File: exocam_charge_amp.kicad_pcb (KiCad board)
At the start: 2 copper layers, 20.3 x 19 mm, 13 parts, among them J1 dupont2x1, J2 dupont2x1, U1 TLV2771CDBVT

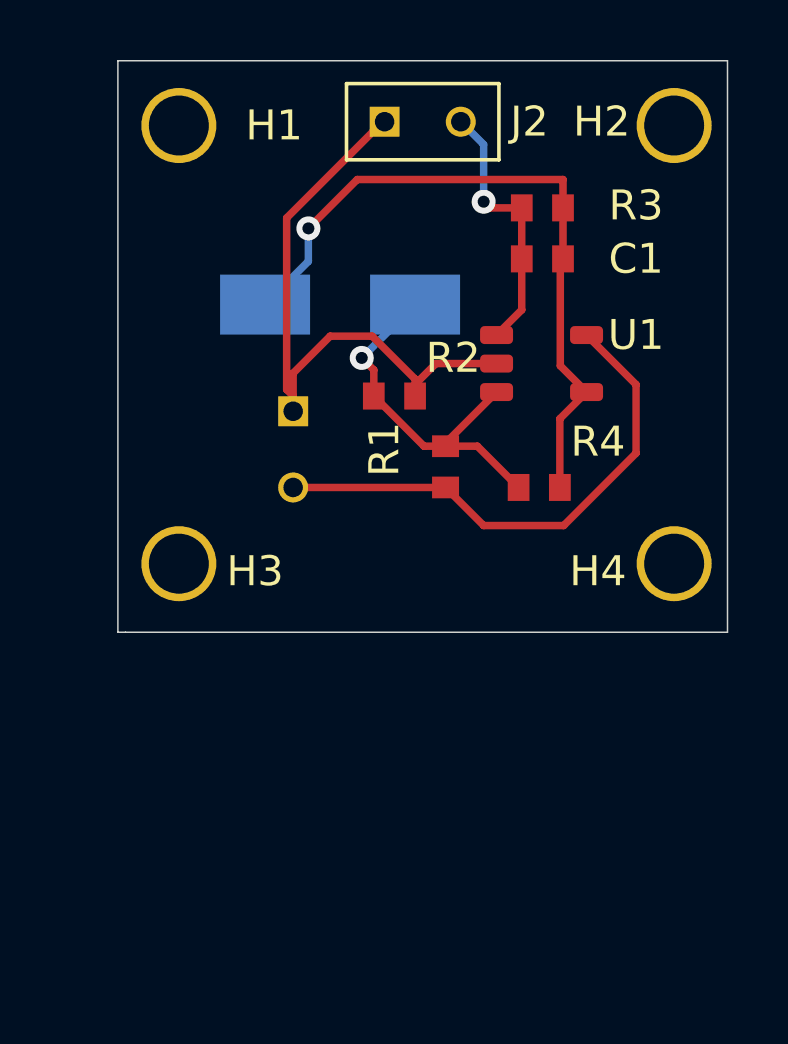
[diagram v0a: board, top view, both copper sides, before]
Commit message: updated pcb to be the new hole pattern on the shoulder side
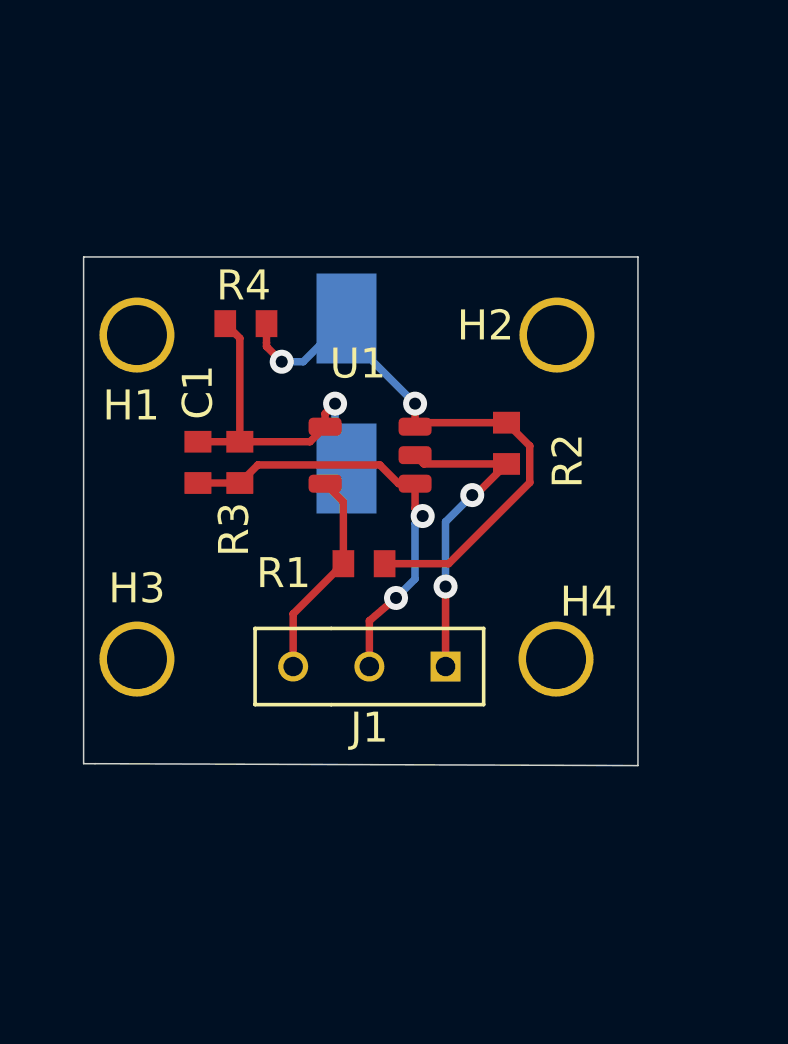
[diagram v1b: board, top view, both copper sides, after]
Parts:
- removed J2: dupont2x1, exocam_charge_amp:dupont2x1
- J1: value dupont2x1 -> dupont3x1; footprint exocam_charge_amp:dupont2x1 -> exocam_charge_amp:dupont3x1; moved to F.Cu
- moved U1 11.3 mm to (61.2, 65.9), turned to 180 degrees
- moved R4 11.0 mm to (56.3, 60.6), turned to 180 degrees
- moved J1 9.91 mm to (61.0, 72.0), turned to 180 degrees
- moved C1 9.65 mm to (57.8, 63.2), turned to 270 degrees
- moved R3 9.54 mm to (59.2, 63.2), turned to 270 degrees
- moved H2 8.00 mm to (68.5, 54.6)
- moved R2 7.38 mm to (68.1, 62.6), turned to 270 degrees
- moved H1 7.12 mm to (54.5, 54.6)
- moved H4 5.06 mm to (68.5, 65.4)
- moved H3 3.47 mm to (54.5, 65.4)
- moved BZ1 2.74 mm to (62.7, 60.3), turned to 90 degrees
- moved R1 1.33 mm to (61.4, 63.5), turned to 0 degrees
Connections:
- J1 pad 2: +5V -> Net-(C1-Pad2)
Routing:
- net Net-(BZ1-Pad1): track 23.3 -> 11.8 mm
- net +5V: track 17.6 -> 7.04 mm
- net GND: track 21.0 -> 10.8 mm, vias 0 -> 2
- net Net-(BZ1-Pad2): track 12.5 -> 20.2 mm, vias 1 -> 2
- net Net-(C1-Pad2): track 8.93 -> 14.9 mm, vias 1 -> 2
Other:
- board size 20.3 x 19 mm -> 18.5 x 17 mm

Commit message: modify board to be the two way amplification stage for higher range of outputs
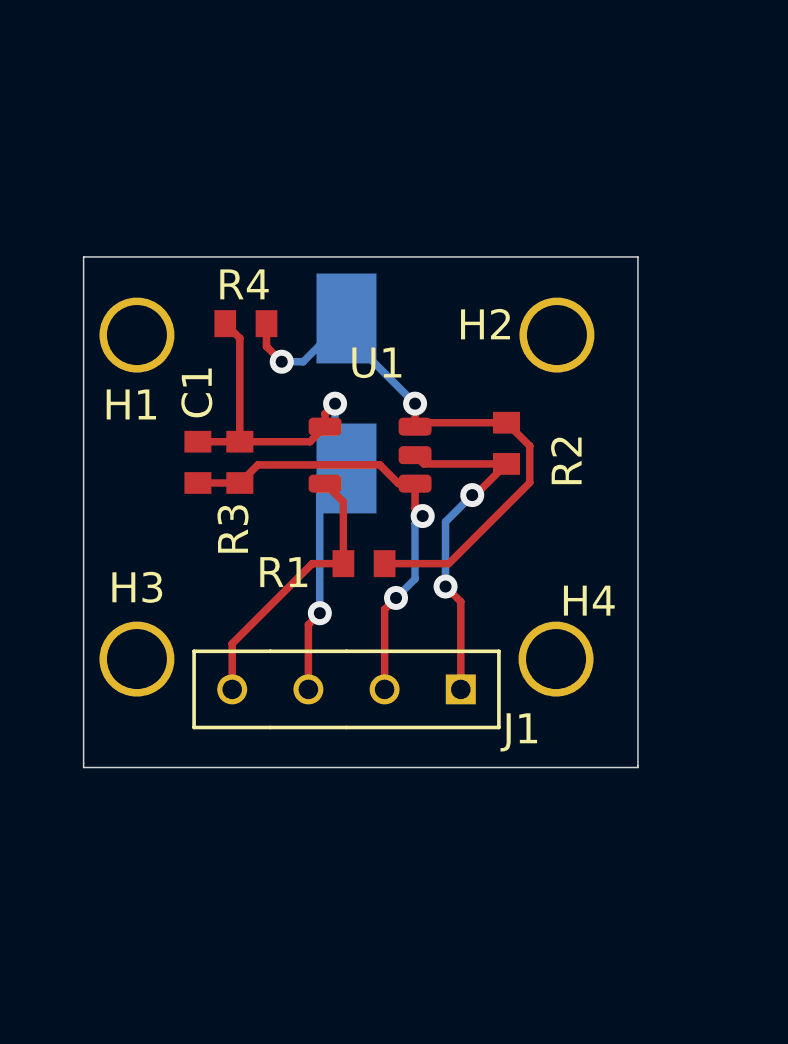
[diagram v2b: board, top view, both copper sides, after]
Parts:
- J1: value dupont3x1 -> dupont4x1; footprint exocam_charge_amp:dupont3x1 -> exocam_charge_amp:dupont4x1
- moved J1 0.92 mm to (61.5, 72.8)
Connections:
- net Net-(C1-Pad2) renamed /Amplified
- BZ1 pad 1: Net-(BZ1-Pad1) -> /UnAmplified
- C1 pad 1: Net-(BZ1-Pad1) -> /UnAmplified
- J1 pad 3: +5V -> /UnAmplified
- R3 pad 1: Net-(BZ1-Pad1) -> /UnAmplified
- R4 pad 2: Net-(BZ1-Pad1) -> /UnAmplified
- U1 pad 4: Net-(BZ1-Pad1) -> /UnAmplified
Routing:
- net /UnAmplified: track 0.00 -> 19.7 mm, vias 0 -> 2
- net Net-(BZ1-Pad1): track 11.8 -> 0.00 mm, vias 1 -> 0
- net +5V: track 7.04 -> 9.25 mm
- net GND: track 10.8 -> 11.8 mm
- net /Amplified: track 14.9 -> 15.4 mm
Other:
- outline, holes or cut-outs redrawn

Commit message: updated so that vertical distance is correct for the holes
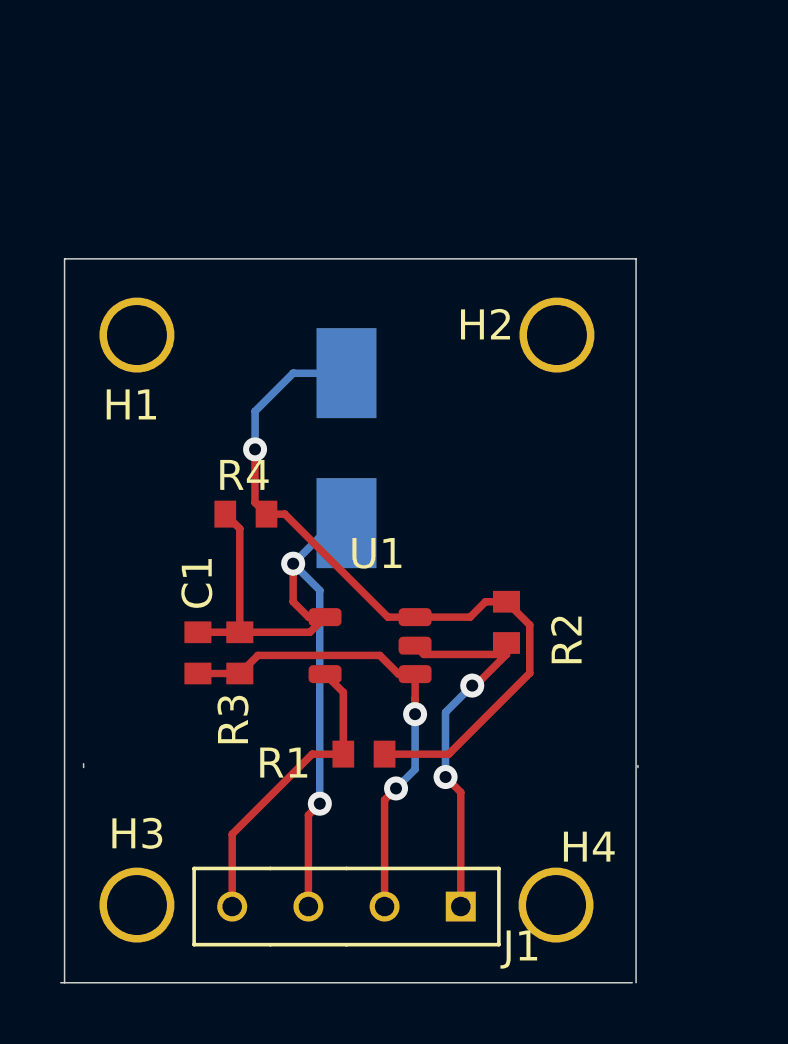
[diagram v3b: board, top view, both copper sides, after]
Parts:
- moved H3 8.20 mm to (54.5, 73.6)
- moved H4 8.20 mm to (68.5, 73.6)
- moved J1 7.24 mm to (61.5, 80.0)
- moved U1 6.35 mm to (61.2, 72.3)
- moved C1 6.35 mm to (57.8, 69.6)
- moved R3 6.35 mm to (59.2, 69.6)
- moved R4 6.35 mm to (56.3, 66.9)
- moved R1 6.35 mm to (61.4, 69.8)
- moved R2 5.97 mm to (68.1, 68.6)
- moved BZ1 1.82 mm to (62.7, 62.1)
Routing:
- net Net-(BZ1-Pad2): track 20.2 -> 26.1 mm, vias 2 -> 1
- net /UnAmplified: track 19.7 -> 25.4 mm
- net GND: track 11.8 -> 12.7 mm
- net +5V: track 9.25 -> 10.1 mm
- net /Amplified: track 15.4 -> 16.0 mm
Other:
- board size 18.5 x 17 mm -> 19.2 x 24.1 mm

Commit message: shoulder silkscreen updated
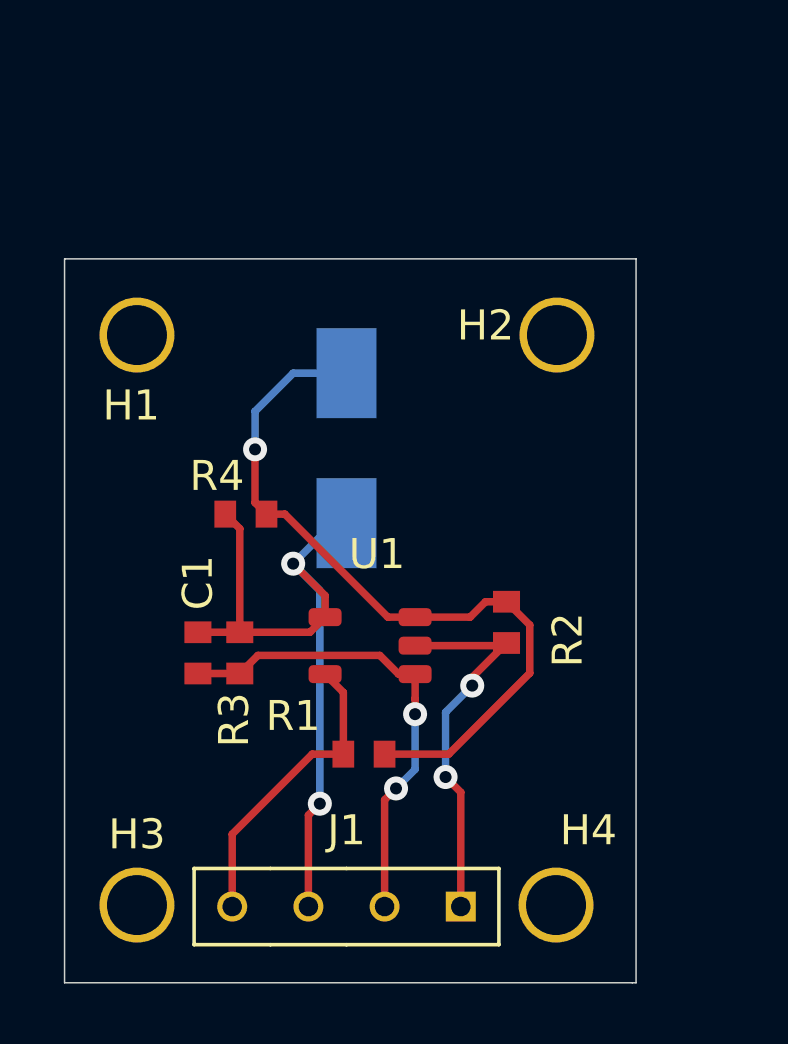
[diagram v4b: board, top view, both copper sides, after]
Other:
- board size 19.2 x 24.1 mm -> 19 x 24.1 mm
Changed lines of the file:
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@@
   (general
     (thickness 1.6)
-    (drawings 6)
+    (drawings 5)
     (tracks 69)
     (zones 0)
@@
   (module exocam_charge_amp:dupont4x1 (layer F.Cu)
     (at 61.468 80.01 180)
-    (fp_text reference J1 (at -4.572 1.2065) (layer F.SilkS)
+    (fp_text reference J1 (at 1.27 5.08) (layer F.SilkS)
       (effects (font (size 1 1) (thickness 0.15)))
     )
@@
   (module exocam_charge_amp:0603_R (layer F.Cu)
     (at 56.261 66.929 180)
-    (fp_text reference R4 (at -0.508 3.81) (layer F.SilkS)
+    (fp_text reference R4 (at 0.381 3.81) (layer F.SilkS)
       (effects (font (size 1 1) (thickness 0.15)))
     )
@@
   (module exocam_charge_amp:0603_R (layer F.Cu)
     (at 61.363 69.85)
-    (fp_text reference R1 (at -3.2605 2.8575) (layer F.SilkS)
+    (fp_text reference R1 (at -2.943 1.27) (layer F.SilkS)
       (effects (font (size 1 1) (thickness 0.15)))
     )
@@
   (module exocam_charge_amp:mount_hole_2.5mm (layer F.Cu)
     (at 68.453 73.61)
-    (fp_text reference H4 (at -0.1905 1.9) (layer F.SilkS)
+    (fp_text reference H4 (at -0.1905 1.32) (layer F.SilkS)
       (effects (font (size 1 1) (thickness 0.15)))
     )
@@
   (module exocam_charge_amp:piezo_buzzer (layer B.Cu)
     (at 62.738 62.15 90)
-    (fp_text reference BZ1 (at 2.286 0.254 90) (layer B.SilkS)
+    (fp_text reference BZ1 (at -0.08 -0.508 90) (layer B.SilkS)
       (effects (font (size 1 1) (thickness 0.15)) (justify mirror))
     )
@@
       (net 4 /UnAmplified))
   )
+  (gr_line (start 50.8 80.01) (end 69.723 80.01) (layer Edge.Cuts) (width 0.05))
+  (gr_line (start 69.723 80.01) (end 69.85 80.01) (layer Edge.Cuts) (width 0.05))
   (gr_line (start 50.8 80.01) (end 50.8 55.88) (layer Edge.Cuts) (width 0.05))
-  (gr_line (start 69.723 80.01) (end 50.673 80.01) (layer Edge.Cuts) (width 0.05))
   (gr_line (start 69.85 55.88) (end 69.85 80.01) (layer Edge.Cuts) (width 0.05))
   (gr_line (start 50.8 55.88) (end 69.85 55.88) (layer Edge.Cuts) (width 0.05))
-  (gr_line (start 69.9135 72.8345) (end 69.9135 72.771) (layer Edge.Cuts) (width 0.05))
-  (gr_line (start 51.435 72.7075) (end 51.435 72.8345) (layer Edge.Cuts) (width 0.05))
   (segment (start 62.616 67.691) (end 62.484 67.823) (width 0.25) (layer F.Cu) (net 1))
   (segment (start 64.319 67.823) (end 62.484 67.823) (width 0.25) (layer F.Cu) (net 1))
@@
   (segment (start 56.388 75.057) (end 59.055 72.39) (width 0.25) (layer F.Cu) (net 2))
   (segment (start 56.388 75.057) (end 56.388 77.47) (width 0.25) (layer F.Cu) (net 2))
-  (segment (start 62.777 69.066) (end 62.484 68.773) (width 0.25) (layer F.Cu) (net 3))
-  (segment (start 65.532 69.066) (end 62.777 69.066) (width 0.25) (layer F.Cu) (net 3))
   (segment (start 63.5 73.152) (end 63.5 73.152) (width 0.25) (layer F.Cu) (net 3))
   (via (at 63.5 73.152) (size 0.8) (drill 0.4) (layers F.Cu B.Cu) (net 3))
@@
   (segment (start 64.389 70.104) (end 64.389 70.104) (width 0.25) (layer B.Cu) (net 3))
   (via (at 64.389 70.104) (size 0.8) (drill 0.4) (layers F.Cu B.Cu) (net 3))
-  (segment (start 64.494 70.104) (end 65.532 69.066) (width 0.25) (layer F.Cu) (net 3))
   (segment (start 64.389 70.104) (end 64.494 70.104) (width 0.25) (layer F.Cu) (net 3))
   (segment (start 64.008 73.66) (end 63.5 73.152) (width 0.25) (layer F.Cu) (net 3))
   (segment (start 64.008 73.66) (end 64.008 77.47) (width 0.25) (layer F.Cu) (net 3))
+  (segment (start 64.389 69.828) (end 65.532 68.685) (width 0.25) (layer F.Cu) (net 3))
+  (segment (start 64.389 70.104) (end 64.389 69.828) (width 0.25) (layer F.Cu) (net 3))
+  (segment (start 65.444 68.773) (end 65.532 68.685) (width 0.25) (layer F.Cu) (net 3))
+  (segment (start 62.484 68.773) (end 65.444 68.773) (width 0.25) (layer F.Cu) (net 3))
   (segment (start 55.245 68.326) (end 56.642 68.326) (width 0.25) (layer F.Cu) (net 4))
   (segment (start 58.981 68.326) (end 59.484 67.823) (width 0.25) (layer F.Cu) (net 4))
@@
   (via (at 59.309 74.041) (size 0.8) (drill 0.4) (layers F.Cu B.Cu) (net 4))
   (segment (start 58.928 74.422) (end 58.928 77.47) (width 0.25) (layer F.Cu) (net 4))
-  (segment (start 59.484 67.823) (end 58.933 67.823) (width 0.25) (layer F.Cu) (net 4))
-  (segment (start 58.933 67.823) (end 58.42 67.31) (width 0.25) (layer F.Cu) (net 4))
-  (segment (start 58.42 67.31) (end 58.42 66.04) (width 0.25) (layer F.Cu) (net 4))
   (segment (start 58.42 66.04) (end 58.42 66.04) (width 0.25) (layer F.Cu) (net 4))
   (via (at 58.42 66.04) (size 0.8) (drill 0.4) (layers F.Cu B.Cu) (net 4))
@@
   (segment (start 59.77 64.69) (end 58.42 66.04) (width 0.25) (layer B.Cu) (net 4))
   (segment (start 60.198 64.69) (end 59.77 64.69) (width 0.25) (layer B.Cu) (net 4))
+  (segment (start 59.484 67.104) (end 58.42 66.04) (width 0.25) (layer F.Cu) (net 4))
+  (segment (start 59.484 67.823) (end 59.484 67.104) (width 0.25) (layer F.Cu) (net 4))
   (segment (start 55.245 69.701) (end 56.642 69.701) (width 0.25) (layer F.Cu) (net 5))
   (segment (start 61.30899 69.09799) (end 61.934 69.723) (width 0.25) (layer F.Cu) (net 5))
